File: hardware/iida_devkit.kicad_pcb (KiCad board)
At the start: 4 copper layers, 0 parts

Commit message: HW: Move VBUS fuse after ESD
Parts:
- added AE1001: Antenna_Shield, PCB_antenna:800MHz_antenna, F.Cu at (142.0, -92.2)
- added C1001: 1.1 pF, perfect_footprints:C_0402_1005Metric, F.Cu at (139.0, -89.2)
- added C1002: 36 pF, perfect_footprints:C_0402_1005Metric, F.Cu at (139.0, -87.3)
- added C1003: 0.33 pF, perfect_footprints:C_0402_1005Metric, F.Cu at (139.0, -85.3)
- added C1004: 36 pF, perfect_footprints:C_0402_1005Metric, F.Cu at (139.0, -83.3)
- added C1005: 1.1 pF, perfect_footprints:C_0402_1005Metric, F.Cu at (139.0, -81.3)
- added C201: 0.1 µF, perfect_footprints:C_0402_1005Metric, F.Cu at (132.9, -34.6)
- added C202: 0.1 µF, perfect_footprints:C_0402_1005Metric, F.Cu at (132.9, -32.6)
- added C301: 100 μF, Capacitor_THT:CP_Radial_D5.0mm_P2.00mm, F.Cu at (179.8, -18.5)
- added C302: 0.1 µF, perfect_footprints:C_0402_1005Metric, F.Cu at (188.0, -22.9)
- added C303: 4.7 µF, Capacitor_SMD:C_0603_1608Metric, F.Cu at (199.2, -27.9)
- added C304: 4.7 µF, Capacitor_SMD:C_0603_1608Metric, F.Cu at (199.2, -25.4)
- added C305: 0.1 µF, perfect_footprints:C_0402_1005Metric, F.Cu at (188.0, -21.0)
- added C401: 10 μF, Capacitor_SMD:C_0603_1608Metric, F.Cu at (183.5, -96.3)
- added C402: 10 μF, Capacitor_SMD:C_0603_1608Metric, F.Cu at (183.5, -93.8)
- added C403: 0.1 µF, perfect_footprints:C_0402_1005Metric, F.Cu at (180.1, -96.6)
- added C404: 22 μF, Capacitor_SMD:C_0603_1608Metric, F.Cu at (183.5, -91.3)
- added C405: 22 μF, Capacitor_SMD:C_0603_1608Metric, F.Cu at (183.5, -88.8)
- added C406: 22 μF, Capacitor_SMD:C_0603_1608Metric, F.Cu at (183.5, -86.3)
- added C501: 0.1 µF, perfect_footprints:C_0402_1005Metric, F.Cu at (139.0, -56.0)
- added C502: 4.7 µF, Capacitor_SMD:C_0603_1608Metric, F.Cu at (171.6, -65.9)
- added C503: 0.1 µF, perfect_footprints:C_0402_1005Metric, F.Cu at (139.0, -54.0)
- added C504: 0.1 µF, perfect_footprints:C_0402_1005Metric, F.Cu at (139.0, -52.0)
- added C505: 8 pF, perfect_footprints:C_0402_1005Metric, F.Cu at (139.0, -50.1)
- added C506: 8 pF, perfect_footprints:C_0402_1005Metric, F.Cu at (139.0, -48.1)
- added C507: 0.1 µF, perfect_footprints:C_0402_1005Metric, F.Cu at (139.0, -46.1)
- added C508: 0.1 µF, perfect_footprints:C_0402_1005Metric, F.Cu at (139.0, -44.1)
- added C509: 0.01 μF, perfect_footprints:C_0402_1005Metric, F.Cu at (141.9, -56.0)
- added C510: 8 pF, perfect_footprints:C_0402_1005Metric, F.Cu at (141.9, -54.0)
- added C511: 8 pF, perfect_footprints:C_0402_1005Metric, F.Cu at (141.9, -52.0)
- added C512: 0.1 µF, perfect_footprints:C_0402_1005Metric, F.Cu at (141.9, -50.1)
- added C513: 4.7 µF, Capacitor_SMD:C_0603_1608Metric, F.Cu at (171.6, -63.4)
- added C514: 0.1 µF, perfect_footprints:C_0402_1005Metric, F.Cu at (141.9, -48.1)
- added C601: 0.1 µF, perfect_footprints:C_0402_1005Metric, F.Cu at (165.1, -33.7)
- added C602: 0.1 µF, perfect_footprints:C_0402_1005Metric, F.Cu at (165.1, -31.7)
- added C701: 0.1 µF, perfect_footprints:C_0402_1005Metric, F.Cu at (126.8, -53.1)
- added C801: 0.1 µF, perfect_footprints:C_0402_1005Metric, F.Cu at (201.7, -61.1)
- added C802: 10 μF, Capacitor_SMD:C_0603_1608Metric, F.Cu at (179.4, -45.5)
- added C803: 0.1 µF, perfect_footprints:C_0402_1005Metric, F.Cu at (201.7, -59.1)
- added C804: 0.1 µF, perfect_footprints:C_0402_1005Metric, F.Cu at (201.7, -57.1)
- added C805: 0.01 μF, perfect_footprints:C_0402_1005Metric, F.Cu at (201.7, -55.1)
- added C806: 68 pF, perfect_footprints:C_0402_1005Metric, F.Cu at (201.7, -53.2)
- added C807: 15 pF, perfect_footprints:C_0402_1005Metric, F.Cu at (204.6, -61.1)
- added C901: 47 pF, perfect_footprints:C_0402_1005Metric, F.Cu at (160.2, -33.7)
- added C902: 47 pF, perfect_footprints:C_0402_1005Metric, F.Cu at (160.2, -31.7)
- added C903: 47 pF, perfect_footprints:C_0402_1005Metric, F.Cu at (160.2, -29.7)
- added C904: 0.1 µF, perfect_footprints:C_0402_1005Metric, F.Cu at (160.2, -27.7)
- added D1001: DF2B5M4CT,L3F, Diode_SMD:D_SOD-882D, F.Cu at (147.7, -79.7)
- added D301: 150141RS73100, LED_SMD:LED_PLCC_2835, F.Cu at (189.3, -34.8)
- added D302: 150141RS73100, LED_SMD:LED_PLCC_2835, F.Cu at (189.3, -30.5)
- added D303: 150141RS73100, LED_SMD:LED_PLCC_2835, F.Cu at (189.3, -26.1)
- added D401: 150141RS73100, LED_SMD:LED_PLCC_2835, F.Cu at (199.0, -84.4)
- added D402: 150141RS73100, LED_SMD:LED_PLCC_2835, F.Cu at (199.0, -80.1)
- added D701: 150141RS73100, LED_SMD:LED_PLCC_2835, F.Cu at (122.6, -52.0)
- added D702: 150141RS73100, LED_SMD:LED_PLCC_2835, F.Cu at (122.6, -47.6)
- added D703: 150141RS73100, LED_SMD:LED_PLCC_2835, F.Cu at (122.6, -43.3)
- added D801: 150141RS73100, LED_SMD:LED_PLCC_2835, F.Cu at (184.2, -44.6)
- added D901: DF2B5M4CT,L3F, Diode_SMD:D_SOD-882D, F.Cu at (157.3, -33.5)
- added D902: DF2B5M4CT,L3F, Diode_SMD:D_SOD-882D, F.Cu at (157.3, -31.2)
- added D903: DF2B5M4CT,L3F, Diode_SMD:D_SOD-882D, F.Cu at (157.3, -28.8)
- added D904: DF2B5M4CT,L3F, Diode_SMD:D_SOD-882D, F.Cu at (157.3, -26.5)
- added D905: DF2B5M4CT,L3F, Diode_SMD:D_SOD-882D, F.Cu at (157.3, -24.2)
- added F201: 1.5A, Fuse:Fuse_0805_2012Metric, B.Cu at (73.6, -30.4)
- added F301: 1.5A, Fuse:Fuse_0805_2012Metric, F.Cu at (194.6, -12.6)
- added FB201: BLM18EG221SN1D, Inductor_SMD:L_0603_1608Metric, F.Cu at (131.4, -23.1)
- added FB801: BLM18EG221SN1D, Inductor_SMD:L_0603_1608Metric, F.Cu at (179.4, -43.0)
- added FID101: Fiducial, Fiducial:Fiducial_1mm_Mask2mm, F.Cu at (142.4, -217.1)
- added FID102: Fiducial, Fiducial:Fiducial_1mm_Mask2mm, F.Cu at (142.4, -213.5)
- added FID103: Fiducial, Fiducial:Fiducial_1mm_Mask2mm, F.Cu at (142.4, -210.0)
- added H101: MountingHole_Pad, MountingHole:MountingHole_5.3mm_M5_Pad_Via, F.Cu at (134.6, -212.8)
- added H102: MountingHole_Pad, MountingHole:MountingHole_5.3mm_M5_Pad_Via, F.Cu at (134.6, -200.6)
- added H103: MountingHole_Pad, MountingHole:MountingHole_5.3mm_M5_Pad_Via, F.Cu at (134.6, -188.5)
- added H104: MountingHole_Pad, MountingHole:MountingHole_5.3mm_M5_Pad_Via, F.Cu at (134.6, -176.3)
- added J1001: 132134, Connector_Coaxial:SMA_Amphenol_132134-11_Vertical, F.Cu at (150.9, -85.5)
- added J201: USB4085-GF-A, Connector_USB:USB_C_Receptacle_GCT_USB4085, F.Cu at (70.6, -21.2)
- added J301: B2B-XH-A, Connector_JST:JST_XH_B2B-XH-A_1x02_P2.50mm_Vertical, F.Cu at (195.6, -33.6)
- added J302: PRPC001DAAN-RC, Connector_PinHeader_2.54mm:PinHeader_1x02_P2.54mm_Vertical, F.Cu at (200.1, -21.6)
- added J401: PRPC001DAAN-RC, Connector_PinHeader_2.54mm:PinHeader_1x02_P2.54mm_Vertical, F.Cu at (180.9, -102.4)
- added J402: 61300111121, Connector_PinHeader_2.54mm:PinHeader_1x01_P2.54mm_Vertical, F.Cu at (193.9, -84.3)
- added J403: 61300111121, Connector_PinHeader_2.54mm:PinHeader_1x01_P2.54mm_Vertical, F.Cu at (193.9, -79.7)
- added J404: PRPC001DAAN-RC, Connector_PinHeader_2.54mm:PinHeader_1x02_P2.54mm_Vertical, F.Cu at (185.5, -102.4)
- added J405: PRPC001DAAN-RC, Connector_PinHeader_2.54mm:PinHeader_1x02_P2.54mm_Vertical, F.Cu at (190.1, -102.4)
- added J406: PRPC001DAAN-RC, Connector_PinHeader_2.54mm:PinHeader_1x02_P2.54mm_Vertical, F.Cu at (194.7, -102.4)
- added J501: PRPC006SAAN-RC, Connector_PinHeader_2.54mm:PinHeader_1x06_P2.54mm_Vertical, F.Cu at (139.8, -72.0)
- added J502: TC2050, Connector:Tag-Connect_TC2050-IDC-NL_2x05_P1.27mm_Vertical_with_bottom_clip, F.Cu at (167.6, -44.6)
- added J503: 61300611121, Connector_PinHeader_2.54mm:PinHeader_1x06_P2.54mm_Vertical, F.Cu at (144.4, -72.0)
- added J504: 61300611121, Connector_PinHeader_2.54mm:PinHeader_1x06_P2.54mm_Vertical, F.Cu at (149.0, -72.0)
- added J505: 61300611121, Connector_PinHeader_2.54mm:PinHeader_1x06_P2.54mm_Vertical, F.Cu at (153.6, -72.0)
- added J506: 61300611121, Connector_PinHeader_2.54mm:PinHeader_1x06_P2.54mm_Vertical, F.Cu at (158.1, -72.0)
- added J507: 61300611121, Connector_PinHeader_2.54mm:PinHeader_1x06_P2.54mm_Vertical, F.Cu at (162.7, -72.0)
- added J508: PRPC001DAAN-RC, Connector_PinHeader_2.54mm:PinHeader_1x02_P2.54mm_Vertical, F.Cu at (171.9, -72.0)
- added J509: PRPC006SAAN-RC, Connector_PinHeader_2.54mm:PinHeader_1x06_P2.54mm_Vertical, F.Cu at (167.3, -72.0)
- added J901: SIM8066-6-1-14-01-A, GCT:SIM8066-6-1-14-01-A, F.Cu at (145.1, -25.5)
- added L1001: 36 nH, perfect_footprints:L_0402_1005Metric, F.Cu at (139.0, -79.3)
- added L1002: 1 nH, perfect_footprints:L_0402_1005Metric, F.Cu at (139.0, -77.3)
- added L1003: 110 nH, perfect_footprints:L_0402_1005Metric, F.Cu at (141.9, -89.2)
- added L1004: 1 nH, perfect_footprints:L_0402_1005Metric, F.Cu at (141.9, -87.3)
- added L1005: 36 nH, perfect_footprints:L_0402_1005Metric, F.Cu at (141.9, -85.3)
- added L401: 1 µH, Inductor_SMD:L_Wuerth_MAPI-4030, F.Cu at (199.8, -101.9)
- added NT301: NetTie_2, NetTie:NetTie-2_SMD_Pad0.5mm, F.Cu at (199.0, -12.4)
- added Q301: IRLML6401TRPBF, Package_TO_SOT_SMD:SOT-23-3, F.Cu at (194.7, -26.8)
- added Q302: DMN2005, Package_SON:Diodes_PowerDI3333-8, F.Cu at (195.2, -21.4)
- added Q303: DMN2005, Package_SON:Diodes_PowerDI3333-8, F.Cu at (195.2, -16.5)
- added Q501: BSS806NH, Package_TO_SOT_SMD:SOT-23-3, F.Cu at (140.1, -40.7)
- added Q801: BSS806NH, Package_TO_SOT_SMD:SOT-23-3, F.Cu at (197.6, -59.7)
- added Q802: IRLML6401TRPBF, Package_TO_SOT_SMD:SOT-23-3, F.Cu at (197.6, -55.1)
- added Q803: BSS806NH, Package_TO_SOT_SMD:SOT-23-3, F.Cu at (197.6, -50.5)
- added Q804: BSS806NH, Package_TO_SOT_SMD:SOT-23-3, F.Cu at (197.6, -45.8)
- added Q805: BSS806NH, Package_TO_SOT_SMD:SOT-23-3, F.Cu at (197.6, -41.2)
- added R1001: 0 Ω, perfect_footprints:R_0402_1005Metric, F.Cu at (141.9, -83.3)
- added R1002: 0 Ω, perfect_footprints:R_0402_1005Metric, F.Cu at (141.9, -81.3)
- added R1003: 0 Ω, Resistor_SMD:R_0402_1005Metric, F.Cu at (141.9, -79.3)
- added R1004: 0 Ω, Resistor_SMD:R_0402_1005Metric, F.Cu at (141.9, -77.3)
- added R1005: 0 Ω, perfect_footprints:R_0402_1005Metric, F.Cu at (144.8, -89.2)
- added R1006: 0 Ω, perfect_footprints:R_0402_1005Metric, F.Cu at (144.8, -87.3)
- added R1007: 0 Ω, Resistor_SMD:R_0402_1005Metric, F.Cu at (144.8, -85.3)
- added R1008: 0 Ω, Resistor_SMD:R_0402_1005Metric, F.Cu at (144.8, -83.3)
- added R201: 5.1 kΩ, perfect_footprints:R_0402_1005Metric, F.Cu at (79.4, -21.3)
- added R202: 5.1 kΩ, perfect_footprints:R_0402_1005Metric, F.Cu at (67.8, -21.3)
- added R301: 330 Ω, perfect_footprints:R_0402_1005Metric, F.Cu at (188.0, -19.0)
- added R302: 82 mΩ, Resistor_SMD:R_1206_3216Metric, F.Cu at (189.3, -12.3)
- added R303: 2.2 kΩ, perfect_footprints:R_0402_1005Metric, F.Cu at (188.0, -17.0)
- added R304: 10 kΩ, perfect_footprints:R_0402_1005Metric, F.Cu at (188.0, -15.0)
- added R305: 2.2 kΩ, perfect_footprints:R_0402_1005Metric, F.Cu at (190.9, -22.9)
- added R306: 4.7 kΩ, perfect_footprints:R_0402_1005Metric, F.Cu at (190.9, -21.0)
- added R307: 4.7 kΩ, perfect_footprints:R_0402_1005Metric, F.Cu at (190.9, -19.0)
- added R308: 4.7 kΩ, perfect_footprints:R_0402_1005Metric, F.Cu at (190.9, -17.0)
- added R309: 22 Ω, perfect_footprints:R_0402_1005Metric, F.Cu at (190.9, -15.0)
- added R401: 0 Ω, Resistor_SMD:R_0402_1005Metric, F.Cu at (180.0, -94.6)
- added R402: 0 Ω, perfect_footprints:R_0402_1005Metric, F.Cu at (180.1, -92.6)
- added R403: 1 MΩ, perfect_footprints:R_0402_1005Metric, F.Cu at (180.1, -90.6)
- added R404: 180 kΩ, perfect_footprints:R_0402_1005Metric, F.Cu at (180.1, -88.6)
- added R405: 0 Ω, perfect_footprints:R_0402_1005Metric, F.Cu at (180.1, -86.6)
- added R406: 4.7 kΩ, perfect_footprints:R_0402_1005Metric, F.Cu at (180.1, -84.7)
- added R407: 2.2 kΩ, perfect_footprints:R_0402_1005Metric, F.Cu at (180.1, -82.7)
- added R501: 22 Ω, perfect_footprints:R_0402_1005Metric, F.Cu at (141.9, -46.1)
- added R502: 180 kΩ, perfect_footprints:R_0402_1005Metric, F.Cu at (141.9, -44.1)
- added R503: 330 Ω, perfect_footprints:R_0402_1005Metric, F.Cu at (144.8, -56.0)
- added R504: 10 kΩ, perfect_footprints:R_0402_1005Metric, F.Cu at (144.8, -54.0)
- added R505: 180 kΩ, perfect_footprints:R_0402_1005Metric, F.Cu at (144.8, -52.0)
- added R506: 330 Ω, perfect_footprints:R_0402_1005Metric, F.Cu at (144.8, -50.1)
- added R507: 330 Ω, perfect_footprints:R_0402_1005Metric, F.Cu at (144.8, -48.1)
- added R508: 10 kΩ, Resistor_SMD:R_0402_1005Metric, F.Cu at (144.8, -46.1)
- added R509: 10 kΩ, perfect_footprints:R_0402_1005Metric, F.Cu at (144.8, -44.1)
- added R510: 22 Ω, perfect_footprints:R_0402_1005Metric, F.Cu at (147.7, -56.0)
- added R511: 22 Ω, perfect_footprints:R_0402_1005Metric, F.Cu at (147.7, -54.0)
- added R512: 4.7 kΩ, perfect_footprints:R_0402_1005Metric, F.Cu at (147.7, -52.0)
- added R513: 4.7 kΩ, perfect_footprints:R_0402_1005Metric, F.Cu at (147.7, -50.1)
- added R514: 0 Ω, Resistor_SMD:R_0603_1608Metric, F.Cu at (171.6, -60.9)
- added R515: 22 Ω, perfect_footprints:R_0402_1005Metric, F.Cu at (147.7, -48.1)
- added R516: 22 Ω, perfect_footprints:R_0402_1005Metric, F.Cu at (147.7, -46.1)
- added R517: 22 Ω, perfect_footprints:R_0402_1005Metric, F.Cu at (147.7, -44.1)
- added R518: 22 Ω, perfect_footprints:R_0402_1005Metric, F.Cu at (150.6, -56.0)
- added R519: 22 Ω, perfect_footprints:R_0402_1005Metric, F.Cu at (150.6, -54.0)
- added R520: 22 Ω, perfect_footprints:R_0402_1005Metric, F.Cu at (150.6, -52.0)
- added R521: 10 kΩ, perfect_footprints:R_0402_1005Metric, F.Cu at (150.6, -50.1)
- added R522: 10 kΩ, Resistor_SMD:R_0603_1608Metric_Pad0.98x0.95mm_HandSolder, F.Cu at (144.8, -41.8)
- added R523: 10 kΩ, Resistor_SMD:R_0603_1608Metric_Pad0.98x0.95mm_HandSolder, F.Cu at (144.8, -39.3)
- added R524: 10 kΩ, perfect_footprints:R_0402_1005Metric, F.Cu at (150.6, -48.1)
- added R601: 180 kΩ, perfect_footprints:R_0402_1005Metric, F.Cu at (165.1, -29.7)
- added R602: 22 Ω, perfect_footprints:R_0402_1005Metric, F.Cu at (165.1, -27.7)
- added R701: 10 kΩ, perfect_footprints:R_0402_1005Metric, F.Cu at (126.8, -51.1)
- added R702: 22 Ω, perfect_footprints:R_0402_1005Metric, F.Cu at (126.8, -49.2)
- added R703: 22 Ω, perfect_footprints:R_0402_1005Metric, F.Cu at (126.8, -47.2)
- added R704: 22 Ω, perfect_footprints:R_0402_1005Metric, F.Cu at (126.8, -45.2)
- added R705: 22 Ω, perfect_footprints:R_0402_1005Metric, F.Cu at (129.7, -53.1)
- added R706: 2.2 kΩ, perfect_footprints:R_0402_1005Metric, F.Cu at (129.7, -51.1)
- added R707: 2.2 kΩ, perfect_footprints:R_0402_1005Metric, F.Cu at (129.7, -49.2)
- added R708: 2.2 kΩ, perfect_footprints:R_0402_1005Metric, F.Cu at (129.7, -47.2)
- added R709: 180 kΩ, perfect_footprints:R_0402_1005Metric, F.Cu at (129.7, -45.2)
- added R801: 180 kΩ, perfect_footprints:R_0402_1005Metric, F.Cu at (204.6, -59.1)
- added R802: 180 kΩ, perfect_footprints:R_0402_1005Metric, F.Cu at (204.6, -57.1)
- added R803: 330 Ω, perfect_footprints:R_0402_1005Metric, F.Cu at (204.6, -55.1)
- added R804: 180 kΩ, perfect_footprints:R_0402_1005Metric, F.Cu at (204.6, -53.2)
- added R805: 330 Ω, perfect_footprints:R_0402_1005Metric, F.Cu at (207.5, -61.1)
- added R806: 2.2 kΩ, perfect_footprints:R_0402_1005Metric, F.Cu at (207.5, -59.1)
- added R807: 22 Ω, perfect_footprints:R_0402_1005Metric, F.Cu at (207.5, -57.1)
- added R808: 180 kΩ, perfect_footprints:R_0402_1005Metric, F.Cu at (207.5, -55.1)
- added R809: 330 Ω, perfect_footprints:R_0402_1005Metric, F.Cu at (207.5, -53.2)
- added R810: 0 Ω, perfect_footprints:R_0402_1005Metric, F.Cu at (210.4, -61.1)
- added R811: 0 Ω, Resistor_SMD:R_0603_1608Metric, F.Cu at (179.4, -40.5)
- added R812: 0 Ω, perfect_footprints:R_0402_1005Metric, F.Cu at (210.4, -59.1)
- added R813: 330 Ω, perfect_footprints:R_0402_1005Metric, F.Cu at (210.4, -57.1)
- added R814: 180 kΩ, perfect_footprints:R_0402_1005Metric, F.Cu at (210.4, -55.1)
- added R815: 2.2 kΩ, perfect_footprints:R_0402_1005Metric, F.Cu at (210.4, -53.2)
- added R901: 10 kΩ, perfect_footprints:R_0402_1005Metric, F.Cu at (160.2, -25.7)
- added SW_SPST501: 430182050816, Button_Switch_SMD:SW_SPST_PTS645, F.Cu at (169.8, -53.1)
- added TP201: TestPoint, TestPoint:TestPoint_Pad_D1.0mm, F.Cu at (182.2, -170.9)
- added TP301: TestPoint, TestPoint:TestPoint_Pad_D1.0mm, F.Cu at (186.1, -184.3)
- added TP302: TestPoint, TestPoint:TestPoint_Pad_D1.0mm, F.Cu at (186.1, -181.3)
- added TP303: TestPoint, TestPoint:TestPoint_Pad_D1.0mm, F.Cu at (186.1, -178.2)
- added TP304: TestPoint, TestPoint:TestPoint_Pad_D1.0mm, F.Cu at (186.1, -175.2)
- added TP305: TestPoint, TestPoint:TestPoint_Pad_D1.0mm, F.Cu at (186.1, -172.1)
- added TP306: TestPoint, TestPoint:TestPoint_Pad_D1.0mm, F.Cu at (189.2, -184.3)
- added TP307: TestPoint, TestPoint:TestPoint_Pad_D1.0mm, F.Cu at (189.2, -181.3)
- added TP308: TestPoint, TestPoint:TestPoint_Pad_D1.0mm, F.Cu at (189.2, -178.2)
- added TP309: TestPoint, TestPoint:TestPoint_Pad_D1.0mm, F.Cu at (189.2, -175.2)
- added TP310: TestPoint, TestPoint:TestPoint_Pad_D1.0mm, F.Cu at (189.2, -172.1)
- added TP311: TestPoint, TestPoint:TestPoint_Pad_D1.0mm, F.Cu at (192.2, -184.3)
- added TP312: TestPoint, TestPoint:TestPoint_Pad_D1.0mm, F.Cu at (192.2, -181.3)
- added TP313: TestPoint, TestPoint:TestPoint_Pad_D1.0mm, F.Cu at (192.2, -178.2)
- added TP401: TestPoint, TestPoint:TestPoint_Pad_D1.0mm, F.Cu at (170.8, -197.5)
- added TP402: TestPoint, TestPoint:TestPoint_Pad_D1.0mm, F.Cu at (170.8, -194.5)
- added TP403: TestPoint, TestPoint:TestPoint_Pad_D1.0mm, F.Cu at (170.8, -191.4)
- added TP404: TestPoint, TestPoint:TestPoint_Pad_D1.0mm, F.Cu at (170.8, -188.4)
- added TP405: TestPoint, TestPoint:TestPoint_Pad_D1.0mm, F.Cu at (173.8, -197.5)
- added TP406: TestPoint, Mechanical:TestPoint_Pad_10.0x10.0mm, F.Cu at (172.7, -207.7)
- added TP407: TestPoint, TestPoint:TestPoint_Pad_D1.0mm, F.Cu at (173.8, -194.5)
- added TP408: TestPoint, TestPoint:TestPoint_Pad_D1.0mm, F.Cu at (173.8, -191.4)
- added TP501: TestPoint, TestPoint:TestPoint_Pad_D1.0mm, F.Cu at (147.9, -181.7)
- added TP502: TestPoint, TestPoint:TestPoint_Pad_D1.0mm, F.Cu at (147.9, -178.6)
- added TP503: TestPoint, TestPoint:TestPoint_Pad_D1.0mm, F.Cu at (147.9, -175.6)
- added TP504: TestPoint, TestPoint:TestPoint_Pad_D1.0mm, F.Cu at (150.9, -181.7)
- added TP505: TestPoint_Small, TestPoint:TestPoint_Pad_D1.0mm, F.Cu at (150.9, -178.6)
- added TP506: TestPoint_Small, TestPoint:TestPoint_Pad_D1.0mm, F.Cu at (150.9, -175.6)
- added TP507: TestPoint_Small, TestPoint:TestPoint_Pad_D1.0mm, F.Cu at (154.0, -181.7)
- added TP508: TestPoint_Small, TestPoint:TestPoint_Pad_D1.0mm, F.Cu at (154.0, -178.6)
- added TP509: TestPoint_Small, TestPoint:TestPoint_Pad_D1.0mm, F.Cu at (154.0, -175.6)
- added TP510: TestPoint_Small, TestPoint:TestPoint_Pad_D1.0mm, F.Cu at (157.0, -181.7)
- added TP511: TestPoint, TestPoint:TestPoint_Pad_D1.0mm, F.Cu at (157.0, -178.6)
- added TP512: TestPoint, TestPoint:TestPoint_Pad_D1.0mm, F.Cu at (157.0, -175.6)
- added TP601: TestPoint, TestPoint:TestPoint_Pad_D1.0mm, F.Cu at (168.8, -167.7)
- added TP701: TestPoint, TestPoint:TestPoint_Pad_D1.0mm, F.Cu at (175.2, -168.3)
- added TP801: TestPoint, TestPoint:TestPoint_Pad_D1.0mm, F.Cu at (165.2, -182.2)
- added TP802: TestPoint, TestPoint:TestPoint_Pad_D1.0mm, F.Cu at (165.2, -179.1)
- added TP803: TestPoint, TestPoint:TestPoint_Pad_D1.0mm, F.Cu at (165.2, -176.1)
- added TP804: TestPoint, TestPoint:TestPoint_Pad_D1.0mm, F.Cu at (165.2, -173.0)
- added TP805: TestPoint, TestPoint:TestPoint_Pad_D1.0mm, F.Cu at (168.2, -182.2)
- added TP806: TestPoint, TestPoint:TestPoint_Pad_D1.0mm, F.Cu at (168.2, -179.1)
- added TP807: TestPoint, TestPoint:TestPoint_Pad_D1.0mm, F.Cu at (168.2, -176.1)
- added TP808: TestPoint, TestPoint:TestPoint_Pad_D1.0mm, F.Cu at (168.2, -173.0)
- added TP809: TestPoint, TestPoint:TestPoint_Pad_D1.0mm, F.Cu at (171.3, -182.2)
- added TP810: TestPoint, TestPoint:TestPoint_Pad_D1.0mm, F.Cu at (171.3, -179.1)
- added TP811: TestPoint, TestPoint:TestPoint_Pad_D1.0mm, F.Cu at (171.3, -176.1)
- added TP812: TestPoint, TestPoint:TestPoint_Pad_D1.0mm, F.Cu at (171.3, -173.0)
- added TP813: TestPoint, TestPoint:TestPoint_Pad_D1.0mm, F.Cu at (174.3, -182.2)
- added TP814: TestPoint, TestPoint:TestPoint_Pad_D1.0mm, F.Cu at (174.3, -179.1)
- added TP815: TestPoint, TestPoint:TestPoint_Pad_D1.0mm, F.Cu at (174.3, -176.1)
- added TP816: TestPoint, TestPoint:TestPoint_Pad_D1.0mm, F.Cu at (174.3, -173.0)
- added TP817: TestPoint, TestPoint:TestPoint_Pad_D1.0mm, F.Cu at (177.4, -182.2)
- added TP818: TestPoint, TestPoint:TestPoint_Pad_D1.0mm, F.Cu at (177.4, -179.1)
- added TP819: TestPoint, TestPoint:TestPoint_Pad_D1.0mm, F.Cu at (177.4, -176.1)
- added TP820: TestPoint, TestPoint:TestPoint_Pad_D1.0mm, F.Cu at (177.4, -173.0)
- added TP901: TestPoint, TestPoint:TestPoint_Pad_D1.0mm, F.Cu at (201.2, -183.5)
- added TP902: TestPoint, TestPoint:TestPoint_Pad_D1.0mm, F.Cu at (201.2, -180.4)
- added TP903: TestPoint, TestPoint:TestPoint_Pad_D1.0mm, F.Cu at (201.2, -177.4)
- added TP904: TestPoint, TestPoint:TestPoint_Pad_D1.0mm, F.Cu at (201.2, -174.3)
- added TP905: TestPoint, TestPoint:TestPoint_Pad_D1.0mm, F.Cu at (201.2, -171.3)
- added U201: USBLC6-2SC6, Package_TO_SOT_SMD:SOT-23-6, B.Cu at (73.6, -25.3)
- added U301: BQ29728DSER, Package_SON:WSON-6_1.5x1.5mm_P0.5mm, F.Cu at (184.8, -13.4)
- added U302: MCP73833T-FCI/MF, Package_DFN_QFN:DFN-10-1EP_3x3mm_P0.5mm_EP1.58x2.35mm, F.Cu at (180.4, -12.8)
- added U303: MAX17048, Package_DFN_QFN:TDFN-8-1EP_2x2mm_P0.5mm_EP0.8x1.2mm, F.Cu at (200.2, -14.9)
- added U401: LM66200DRLR, Package_TO_SOT_SMD:SOT-583-8, F.Cu at (183.3, -83.0)
- added U402: TPS63020DSJR, Texas Instruments:TPS63021DSJR, F.Cu at (188.4, -82.4)
- added U501: STM32L552CEU6, Package_DFN_QFN:QFN-48-1EP_7x7mm_P0.5mm_EP5.6x5.6mm, F.Cu at (156.7, -43.2)
- added U502: AT25SF081B-MAHB-T, Package_DFN_QFN:DFN-8-1EP_2x3mm_P0.5mm_EP0.61x2.2mm, F.Cu at (149.4, -40.8)
- added U601: MCP9808T-E/MC, Package_DFN_QFN:DFN-8-1EP_3x2mm_P0.5mm_EP1.75x1.45mm, F.Cu at (169.3, -32.8)
- added U602: SHT40-AD1B-R2, Sensor_Humidity:Sensirion_DFN-4_1.5x1.5mm_P0.8mm_SHT4x_NoCentralPad, F.Cu at (168.5, -29.4)
- added U701: TCA9554PW, Package_SO:TSSOP-16_4.4x5mm_P0.65mm, F.Cu at (130.1, -40.9)
- added U801: SN74AVC4T774, Package_SO:TSSOP-16_4.4x5mm_P0.65mm, F.Cu at (205.0, -48.9)
- added U802: SARA-R500S-01B, RF_GSM:ublox_SARA_LGA-96, F.Cu at (186.3, -60.5)
- added Y501: ECS-160-9-37-CKM-TR3, Crystal:Crystal_SMD_3225-4Pin_3.2x2.5mm, F.Cu at (164.0, -39.0)
- added Y502: ABS05-32.768KHZ-9-T, Crystal:Crystal_SMD_MicroCrystal_CM9V-T1A-2Pin_1.6x1.0mm, F.Cu at (168.4, -39.7)
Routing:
- net /USB/USB_DP_IN: track 0.00 -> 4.88 mm
- net /USB/USB_DN_IN: track 0.00 -> 4.88 mm
- net /Microcontroller/USB_DP: track 0.00 -> 1.18 mm, vias 0 -> 1
- net /Microcontroller/USB_DN: track 0.00 -> 1.18 mm, vias 0 -> 1
- net GND: vias 0 -> 68
- net /USB/VBUS: vias 0 -> 3

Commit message: HW: Layout USB and Battery
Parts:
- F201, U201: moved to F.Cu
- J201: value USB4085-GF-A -> USB4105-GF-A; footprint Connector_USB:USB_C_Receptacle_GCT_USB4085 -> Connector_USB:USB_C_Receptacle_GCT_USB4105-xx-A_16P_TopMnt_Horizontal
- TP201, TP301, TP302, TP303, TP304, TP305, TP306, TP307, TP308, TP309, TP310, TP311, TP312, TP313: moved to B.Cu
- moved TP301 303.3 mm to (46.2, 84.7)
- moved TP311 300.8 mm to (66.5, 88.9)
- moved TP302 299.7 mm to (48.3, 84.8)
- moved TP312 294.1 mm to (66.4, 84.6)
- moved TP307 293.4 mm to (55.0, 79.7)
- moved TP201 292.9 mm to (64.8, 97.4), turned to -90 degrees
- moved TP310 290.6 mm to (66.4, 91.2)
- moved TP309 288.9 mm to (67.7, 87.0)
- moved TP308 288.6 mm to (65.1, 82.3)
- moved TP306 288.6 mm to (62.6, 75.0)
- moved TP304 287.6 mm to (57.1, 81.9)
- moved TP303 286.6 mm to (50.6, 74.3)
- moved TP313 286.6 mm to (69.2, 80.6)
- moved TP305 278.0 mm to (58.6, 74.9)
- moved J301 187.4 mm to (43.7, 76.2), turned to -90 degrees
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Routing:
- net /Battery/BATT-: track 0.00 -> 22.3 mm, vias 0 -> 1
- net /Battery/BAT_DET: track 0.00 -> 21.2 mm, vias 0 -> 2
- net /Battery/V_BAT: track 0.00 -> 18.1 mm
- net /USB/VBUS: track 0.00 -> 17.0 mm, vias 3 -> 0
- net /Battery/BATT+: track 0.00 -> 9.34 mm
- net /Battery/C_{OUT}: track 0.00 -> 8.32 mm, vias 0 -> 1
- net /USB/CC1: track 0.00 -> 8.30 mm
- net /USB/CC2: track 0.00 -> 7.69 mm
- net /Battery/STAT1: track 0.00 -> 5.75 mm, vias 0 -> 1
- net /Battery/THERM: track 0.00 -> 5.66 mm, vias 0 -> 1
- net /Microcontroller/USB_DN: track 1.18 -> 6.63 mm, vias 1 -> 2
- net /Battery/STAT2: track 0.00 -> 4.83 mm, vias 0 -> 1
- net /Battery/ALRTn: track 0.00 -> 4.50 mm, vias 0 -> 1
- net /Battery/PG: track 0.00 -> 4.22 mm, vias 0 -> 1
- net Net-(Q301-D): track 0.00 -> 3.94 mm, vias 0 -> 1
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- added copper zone on F.Cu, net /Battery/BATT+
- added copper zone on F.Cu, net /Battery/BATT-
- added copper zone on F.Cu, net /Battery/BAT_PROT_IN
- added copper zone on F.Cu, net /Battery/V_5V0
- added copper zone on F.Cu, net /Battery/V_BAT
- added copper zone on F.Cu, net /USB/VBUS_UNFILTERED
- added copper zone on F.Cu, net Net-(Q301-D)
- added copper zone on F.Cu, net Net-(Q302-D)
- added copper zone on F.Cu, net Net-(Q302-S-Pad1)
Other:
- board text added: "ALERTn"
- board text added: "BATT+"
- board text added: "BATT-"
- board text added: "C_{OUT}"
- board text added: "D_{OUT}"
- board text added: "PG"
- board text added: "PROG"
- board text added: "REV_PROT_D"
- board text added: "STAT1"
- board text added: "STAT2"
- board text added: "THERM"
- board text added: "V-"
- board text added: "VBUS_UNFILTERED"
- board text added: "V_BAT"

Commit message: HW: Update libraries
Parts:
- removed the J403 at (193.9, -79.7)
- removed the TP406 at (172.7, -207.7)
- R401: footprint Resistor_SMD:R_0402_1005Metric -> perfect_footprints:R_0402_1005Metric
- TP401, TP402, TP403, TP404, TP405: moved to B.Cu
- U303: value MAX17048 -> MAX17048G+T10
- moved TP407 302.0 mm to (77.2, 94.6)
- moved TP402 301.2 mm to (74.4, 90.8)
- moved TP406 300.8 mm to (84.8, 92.8)
- moved TP405 299.1 mm to (86.1, 88.4)
- moved TP403 297.6 mm to (77.4, 91.1)
- moved TP401 296.0 mm to (73.0, 81.8)
- moved TP404 292.2 mm to (80.0, 89.3)
- moved J401 232.4 mm to (58.1, 94.9)
- moved J405 226.5 mm to (84.8, 95.7)
- moved J404 226.1 mm to (81.2, 95.7)
- moved D401 220.8 mm to (81.2, 102.3), turned to 90 degrees
- moved L401 217.4 mm to (80.9, 80.2), turned to 180 degrees
- moved D402 215.2 mm to (84.8, 102.3), turned to 90 degrees
- moved R406 214.4 mm to (81.2, 105.6), turned to -90 degrees
- moved R407 211.0 mm to (84.8, 105.6), turned to -90 degrees
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- renumbered J404 to J403, J405 to J404, J406 to J405, TP407 to TP406, TP408 to TP407
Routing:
- net /Battery/V_5V0: track 0.00 -> 39.4 mm
- net Net-(D303-K): track 0.00 -> 23.4 mm, vias 0 -> 2
- net /Power/VINA: track 0.00 -> 18.2 mm, vias 0 -> 4
- net Net-(D302-K): track 0.00 -> 16.3 mm, vias 0 -> 2
- net Net-(D301-K): track 0.00 -> 13.9 mm, vias 0 -> 2
- net /Battery/V_BAT: track 18.1 -> 28.6 mm
- net /Power/PS/SYNC: track 0.00 -> 8.26 mm, vias 0 -> 1
- net Net-(U402-FB): track 0.00 -> 6.10 mm, vias 0 -> 1
- net Net-(U402-PG): track 0.00 -> 2.92 mm, vias 0 -> 1
- net V_3V3: track 0.00 -> 2.84 mm
- net /Power/V_SYS: track 0.00 -> 2.77 mm, vias 0 -> 1
- net Net-(D401-A): track 0.00 -> 2.72 mm
- net Net-(D402-A): track 0.00 -> 2.72 mm
- net Net-(D402-K): track 0.00 -> 1.88 mm
- net Net-(D401-K): track 0.00 -> 1.87 mm
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- added copper zone on F.Cu, net /Power/VOUT
- added copper zone on F.Cu, net /Power/V_SYS
- added copper zone on F.Cu, net Net-(L401-Pad1)
- added copper zone on F.Cu, net Net-(L401-Pad2)
- added copper zone on F.Cu, net V_3V3
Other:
- board text added: "+5V>"
- board text added: "3.3V"
- board text added: "5V"
- board text added: "BAT PROT BYPASS"
- board text added: "FB"
- board text added: "GND"
- board text added: "GND>"
- board text added: "PS/SYNC"
- board text added: "VINA"
- board text added: "V_3V3"
- board text added: "V_5V0"
- board text added: "V_SYS"

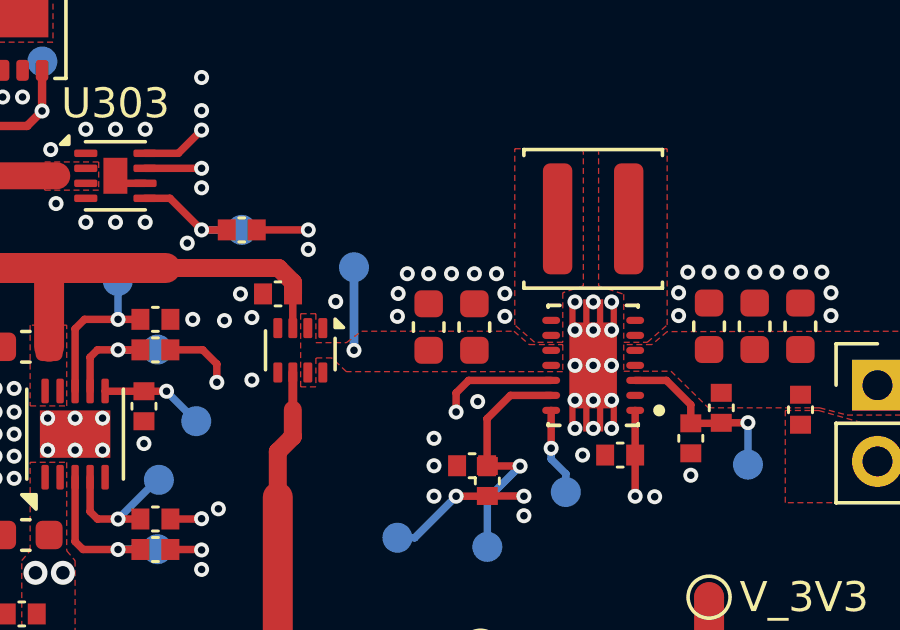
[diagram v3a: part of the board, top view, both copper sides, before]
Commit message: HW: Fix DCDC converter input cap placement
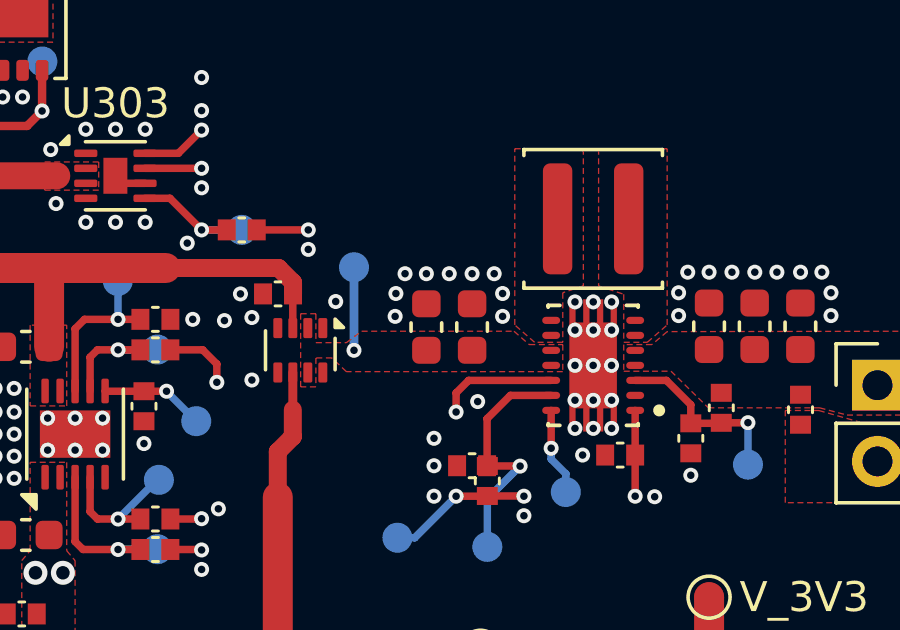
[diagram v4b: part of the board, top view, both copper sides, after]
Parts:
- moved C401 0.08 mm to (75.4, 83.8)
- moved C402 0.08 mm to (76.9, 83.8)
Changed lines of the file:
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@@
 	(footprint "Capacitor_SMD:C_0603_1608Metric"
 		(layer "F.Cu")
-		(at 75.452525 83.8216 90)
+		(at 75.376325 83.8216 90)
 		(descr "Capacitor SMD 0603 (1608 Metric), square (rectangular) end terminal, IPC-7351 nominal, (Body size source: IPC-SM-782 page 76, https://www.pcb-3d.com/wordpress/wp-content/uploads/ipc-sm-782a_amendment_1_and_2.pdf), generated with kicad-footprint-generator")
 		(tags "capacitor")
@@
 	(footprint "Capacitor_SMD:C_0603_1608Metric"
 		(layer "F.Cu")
-		(at 76.976525 83.8216 90)
+		(at 76.900325 83.8216 90)
 		(descr "Capacitor SMD 0603 (1608 Metric), square (rectangular) end terminal, IPC-7351 nominal, (Body size source: IPC-SM-782 page 76, https://www.pcb-3d.com/wordpress/wp-content/uploads/ipc-sm-782a_amendment_1_and_2.pdf), generated with kicad-footprint-generator")
 		(tags "capacitor")
@@
 	)
 	(via
-		(at 74.411125 83.466)
+		(at 74.334925 83.466)
 		(size 0.5)
 		(drill 0.25)
@@
 	)
 	(via
-		(at 75.452525 82.0436)
+		(at 75.376325 82.0436)
 		(size 0.5)
 		(drill 0.25)
@@
 	)
 	(via
-		(at 77.992525 82.704)
+		(at 77.916325 82.704)
 		(size 0.5)
 		(drill 0.25)
@@
 	)
 	(via
-		(at 76.976525 82.0436)
+		(at 76.900325 82.0436)
 		(size 0.5)
 		(drill 0.25)
@@
 	)
 	(via
-		(at 77.713125 82.0436)
+		(at 77.636925 82.0436)
 		(size 0.5)
 		(drill 0.25)
@@
 	)
 	(via
-		(at 76.214525 82.0436)
+		(at 76.138325 82.0436)
 		(size 0.5)
 		(drill 0.25)
@@
 	)
 	(via
-		(at 77.992525 83.466)
+		(at 77.916325 83.466)
 		(size 0.5)
 		(drill 0.25)
@@
 	)
 	(via
-		(at 74.436525 82.704)
+		(at 74.360325 82.704)
 		(size 0.5)
 		(drill 0.25)
@@
 	)
 	(via
-		(at 74.741325 82.0436)
+		(at 74.665125 82.0436)
 		(size 0.5)
 		(drill 0.25)

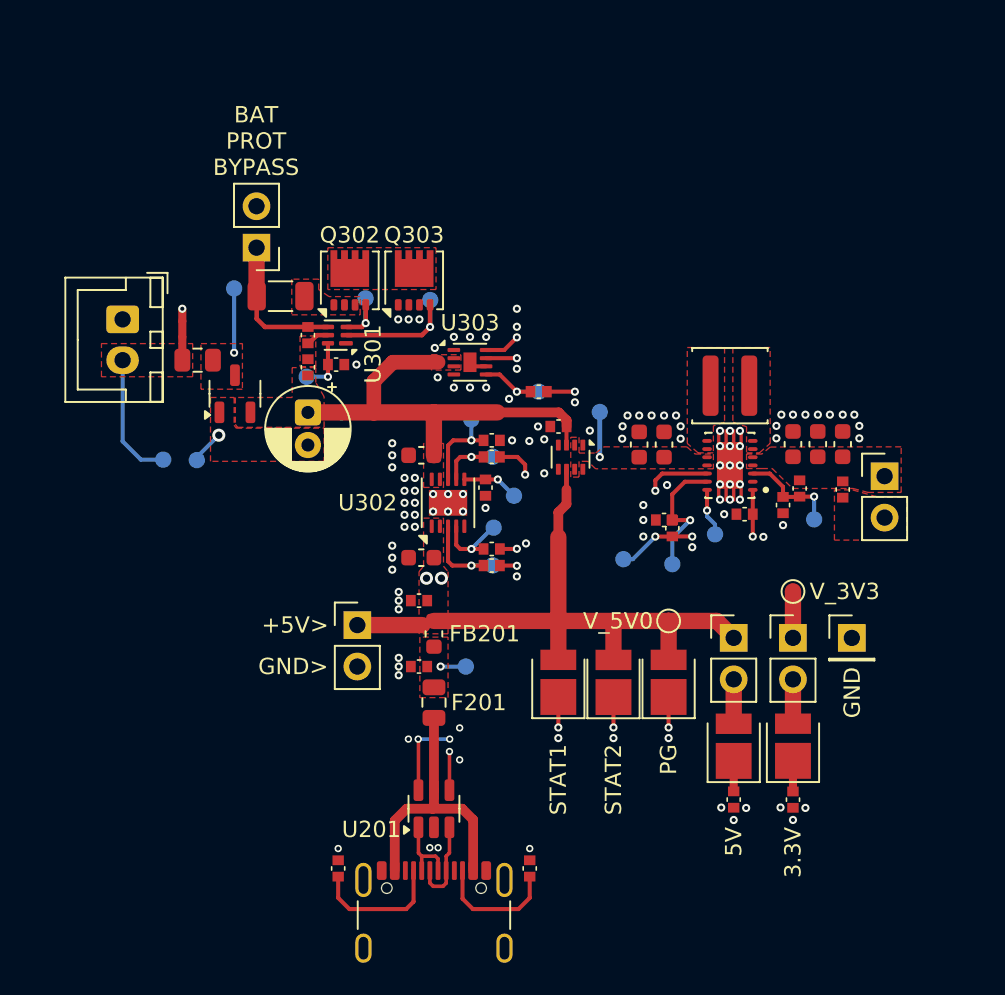
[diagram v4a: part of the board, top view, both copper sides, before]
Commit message: HW: Refine power section
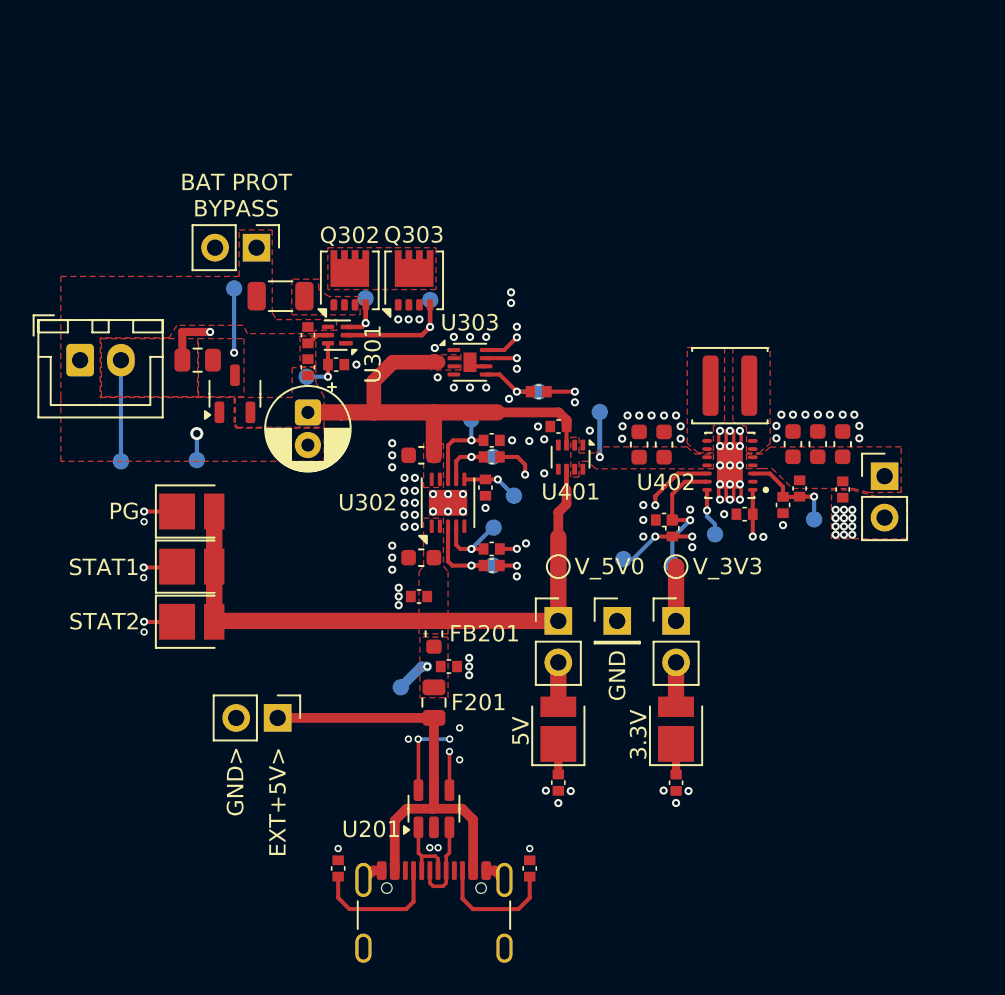
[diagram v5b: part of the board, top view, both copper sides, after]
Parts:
- removed the J401 at (58.1, 94.9)
- added J202: PRPC001DAAN-RC, Connector_PinHeader_2.54mm:PinHeader_1x02_P2.54mm_Vertical, F.Cu at (53.2, 100.6)
- moved D303 31.0 mm to (48.0, 87.9), turned to 0 degrees
- moved D302 26.1 mm to (48.0, 94.7), turned to 0 degrees
- moved D301 23.5 mm to (48.0, 91.3), turned to 0 degrees
- moved J401 14.4 mm to (74.0, 94.6)
- moved D401 10.8 mm to (70.4, 101.3)
- moved J403 10.8 mm to (70.4, 94.6)
- moved R406 10.8 mm to (70.4, 104.5)
- moved TP407 7.53 mm to (70.4, 91.3)
- moved TP406 7.32 mm to (77.6, 91.3)
- moved D402 7.24 mm to (77.6, 101.3)
- moved J404 7.24 mm to (77.6, 94.6)
- moved R407 7.24 mm to (77.6, 104.5)
- moved TP201 4.19 mm to (60.8, 98.7)
- moved J301 3.61 mm to (41.1, 78.7), turned to 0 degrees
- moved TP301 2.59 mm to (43.6, 84.9)
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- renumbered J402 to J401, J403 to J402, J404 to J403, J405 to J404
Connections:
- net /Battery/BAT_INTn renamed /Battery/BAT_MON_INTn
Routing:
- net /Battery/BATT-: track 22.3 -> 1.63 mm
- net Net-(D302-K): track 16.3 -> 31.3 mm
- net Net-(D301-K): track 13.9 -> 26.6 mm
- net /USB/VBUS: track 17.0 -> 27.3 mm
- net Net-(D303-K): track 23.4 -> 30.1 mm
- net GND: track 1.09 -> 3.81 mm, vias 112 -> 110
- net /Battery/V_5V0: track 39.4 -> 37.3 mm, vias 2 -> 0
- net /Battery/BATT+: track 9.34 -> 7.93 mm
- net /Battery/BAT_DET: track 21.2 -> 20.2 mm
- net /USB/VBUS_UNFILTERED: track 1.55 -> 2.15 mm, vias 1 -> 4
- net /Power/VINA: track 18.2 -> 17.6 mm
- net V_3V3: track 2.84 -> 3.33 mm, vias 0 -> 12
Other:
- board text added: "EXT+5V>"
- board text added: "SYS_PG"
- board text removed: "+5V>"
